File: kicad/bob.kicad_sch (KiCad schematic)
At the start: 45 parts, among them J1 GPIO (Optional), J2 Mini USB Female, J3 Battery Connector, J4 GPIO (Optional), SW1 Screw Switch, U1 RP2040, U2 W25Q64JVSS, U3 NCP1117-3.3_SOT223, U4 MPU-6050, Y1 12MHz

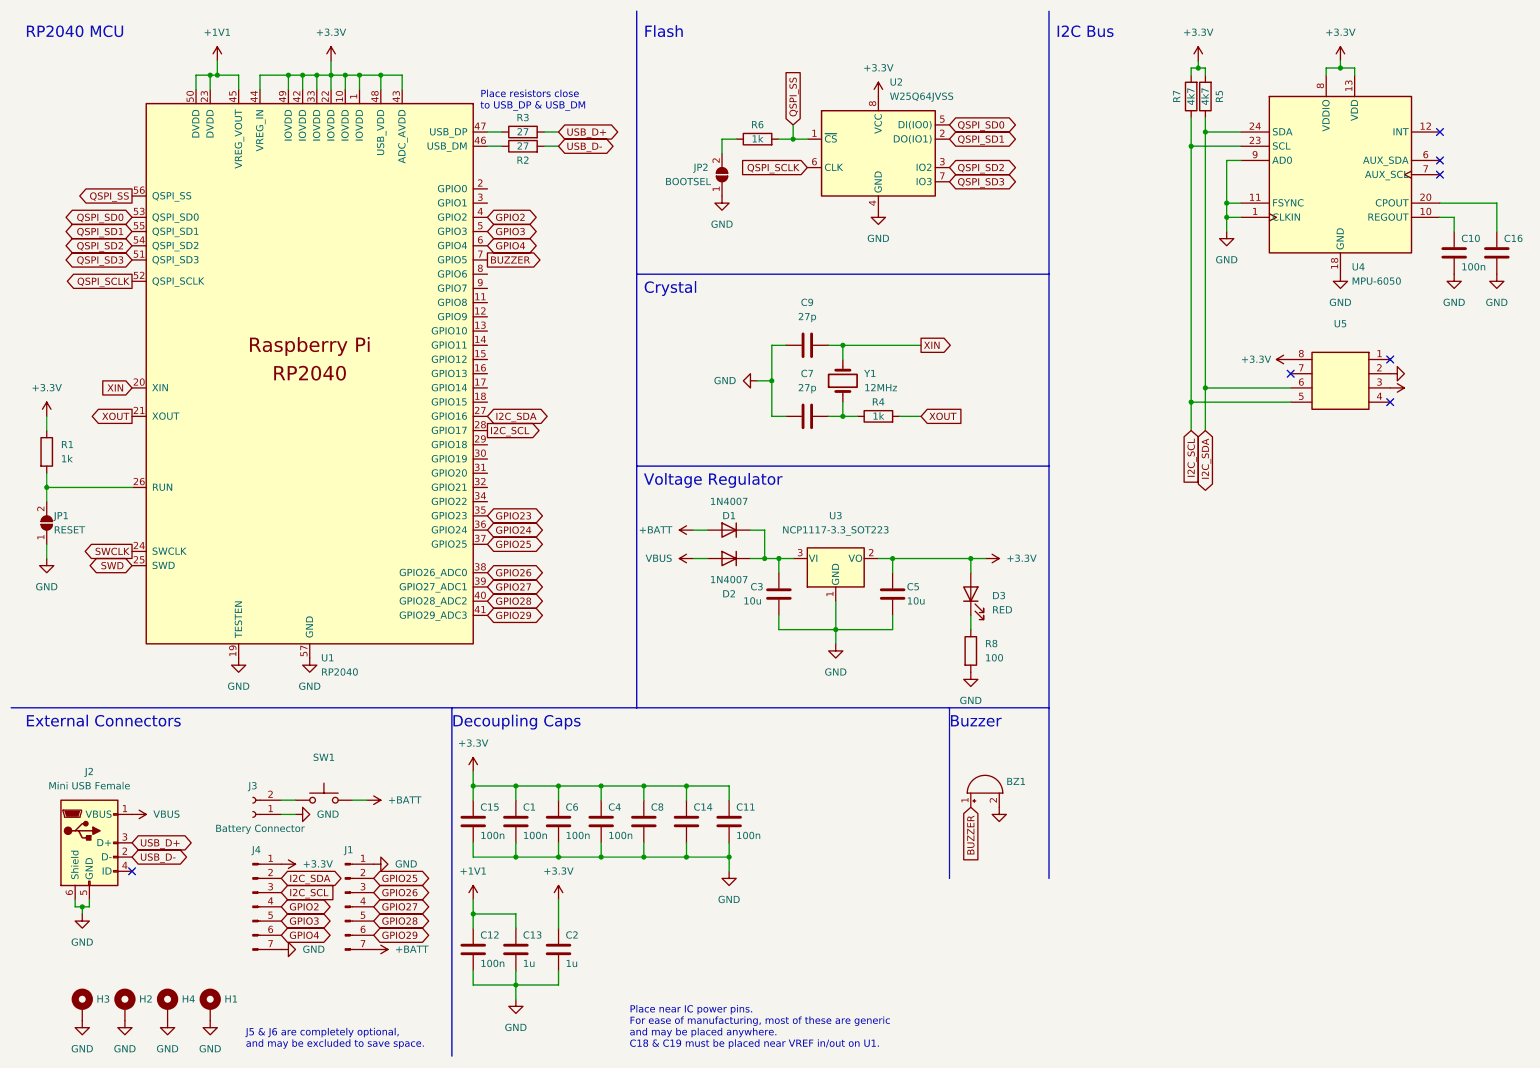
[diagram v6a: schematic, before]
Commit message: Added SWD connector and test points
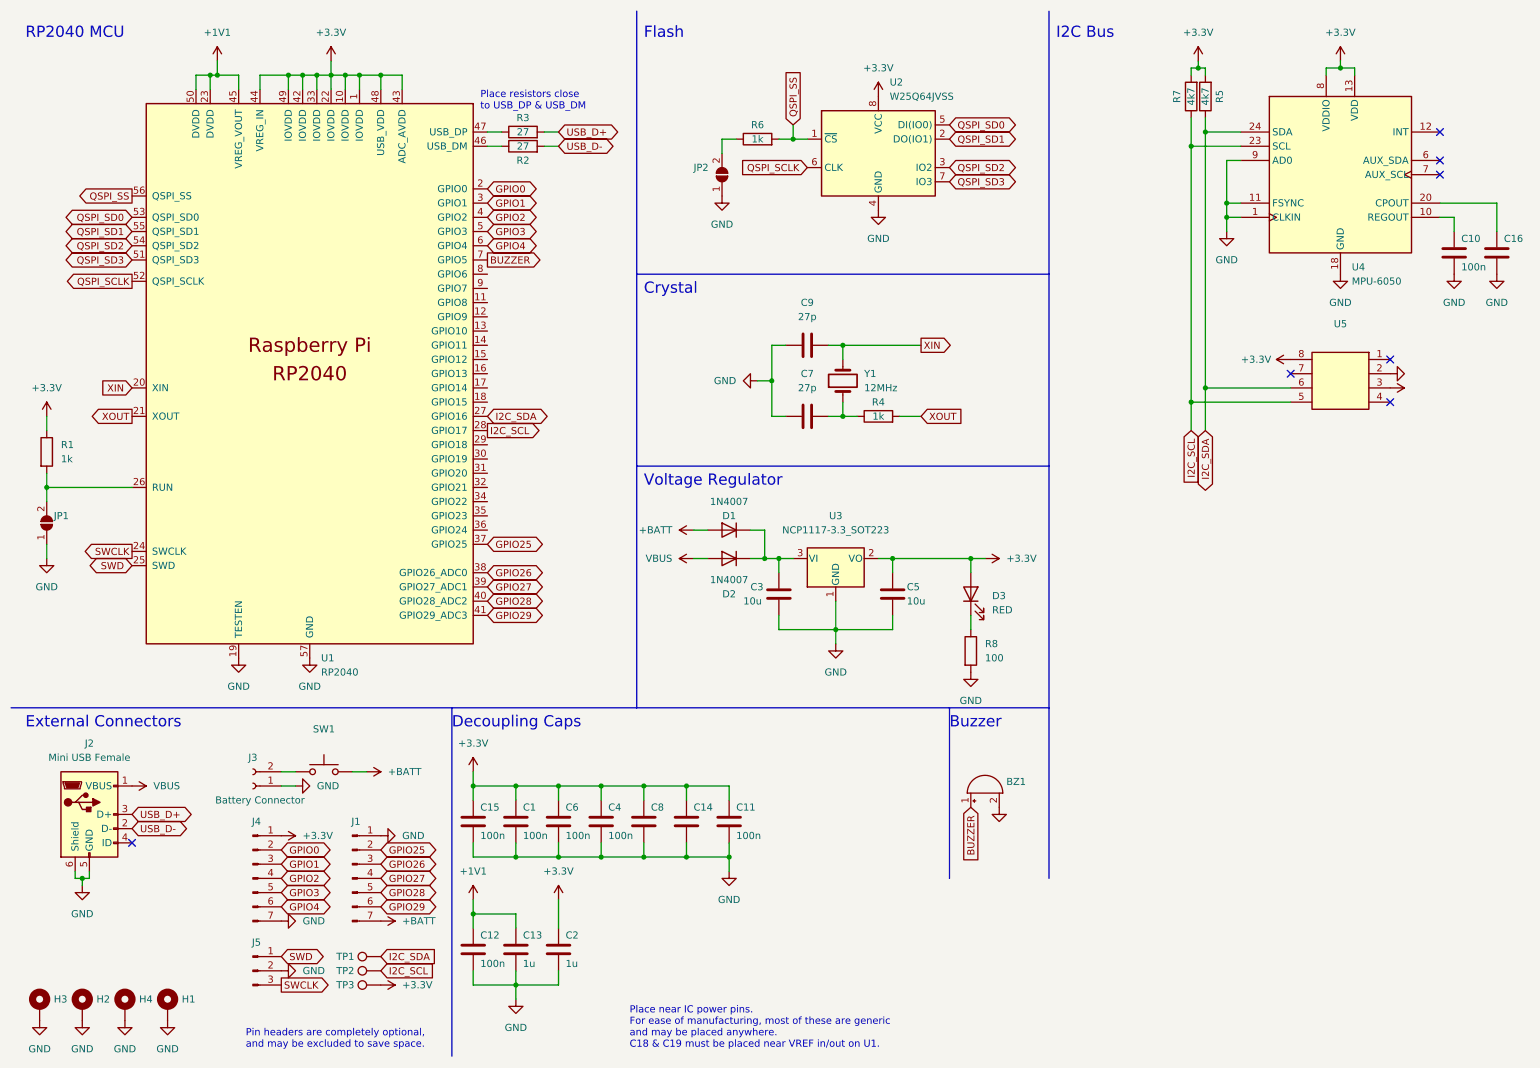
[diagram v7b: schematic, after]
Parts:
- added J5: (no value), symbol Connector:Conn_01x03_Male
- added TP1, TP2, TP3: (no value), symbol Connector:TestPoint
- C1, C10, C11, C12, C13, C15, C2, C4, C6, C7, C9: footprint Capacitor_SMD:C_0402_1005Metric -> (none)
- JP1: value RESET -> (none); footprint Jumper:SolderJumper-2_P1.3mm_Open_TrianglePad1.0x1.5mm -> (none)
- JP2: value BOOTSEL -> (none); footprint Jumper:SolderJumper-2_P1.3mm_Open_TrianglePad1.0x1.5mm -> (none)
- R1, R2, R3, R4, R5, R6, R7, R8: footprint Resistor_SMD:R_0402_1005Metric -> (none)
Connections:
- net +3V3: now also TP3.1
- net GND: now also J5.2 (Pin_2)
- net I2C_SCL: now also TP2.1; no longer J4.3 (Pin_3)
- net I2C_SDA: now also TP1.1; no longer J4.2 (Pin_2)
- net SWCLK: now also J5.3 (Pin_3)
- net SWD: now also J5.1 (Pin_1)
- net GPIO0: now reaches U1.2 (GPIO0)
- net GPIO0: now also J4.2 (Pin_2)
- net GPIO1: now reaches U1.3 (GPIO1)
- net GPIO1: now also J4.3 (Pin_3)
- net GPIO23: no longer names the net of U1.35 (GPIO23)
- net GPIO24: no longer names the net of U1.36 (GPIO24)
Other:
- note added: "Pin headers are completely optional, and may be excluded to save space."
- note removed: "J5 & J6 are completely optional, and may be excluded to save space."
- moved on the sheet: H1, H2, H3, H4, J1, J2, J3, J4, SW1

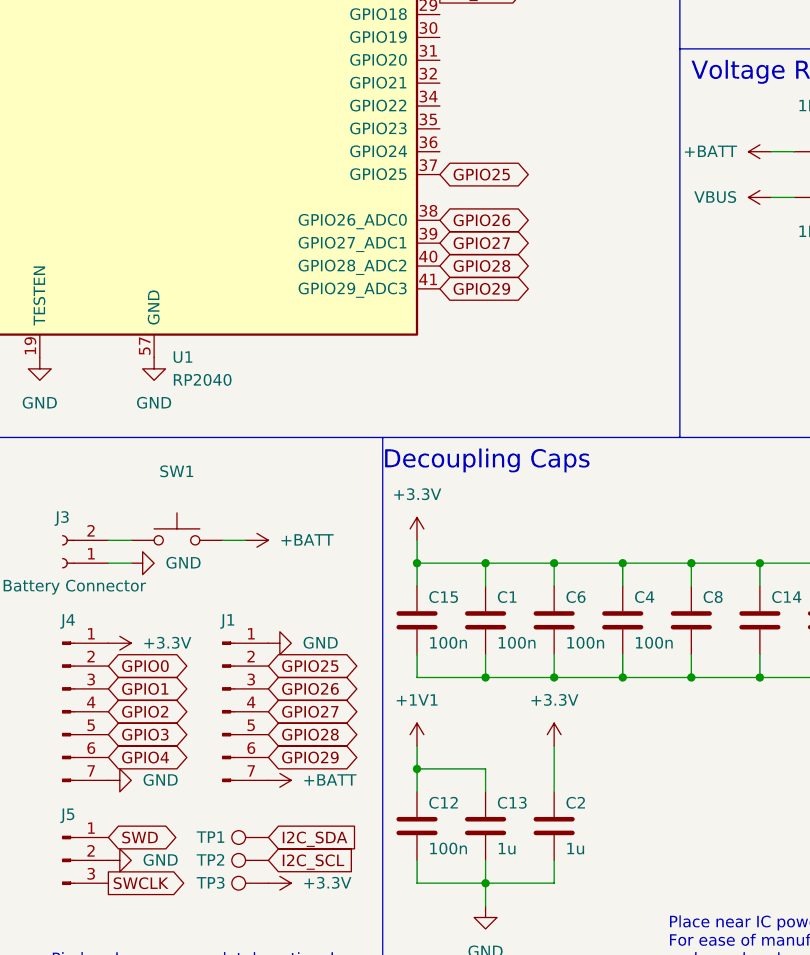
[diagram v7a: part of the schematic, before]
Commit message: Broke out VBAT
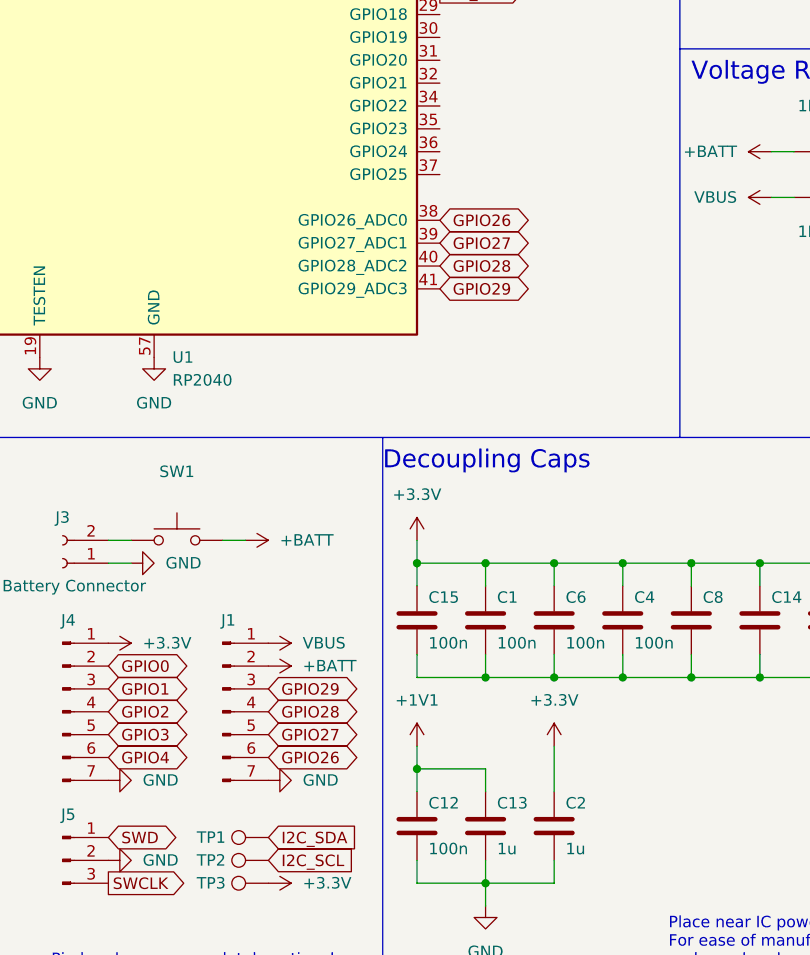
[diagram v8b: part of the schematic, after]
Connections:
- net +BATT: now also J1.2 (Pin_2); no longer J1.7 (Pin_7)
- net GND: now also J1.7 (Pin_7); no longer J1.1 (Pin_1)
- net GPIO26: now also J1.6 (Pin_6); no longer J1.3 (Pin_3)
- net GPIO27: now also J1.5 (Pin_5); no longer J1.4 (Pin_4)
- net GPIO28: now also J1.4 (Pin_4); no longer J1.5 (Pin_5)
- net GPIO29: now also J1.3 (Pin_3); no longer J1.6 (Pin_6)
- net VBUS: now also J1.1 (Pin_1)
- net GPIO25: no longer names the net of U1.37 (GPIO25)
- net GPIO25: no longer J1.2 (Pin_2)
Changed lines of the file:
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@@
+    )
+  )
+  (global_label "GPIO26" (shape bidirectional) (at 76.2 171.45 0) (fields_autoplaced)
+    (effects (font (size 1.27 1.27)) (justify left))
+    (property "Intersheet References" "${INTERSHEET_REFS}" (id 0) (at 85.5074 171.5294 0)
+      (effects (font (size 1.27 1.27)) (justify left) hide)
     )
   )
@@
     )
   )
-  (global_label "GPIO29" (shape bidirectional) (at 76.2 171.45 0) (fields_autoplaced)
-    (effects (font (size 1.27 1.27)) (justify left))
-    (property "Intersheet References" "${INTERSHEET_REFS}" (id 0) (at 85.5074 171.3706 0)
-      (effects (font (size 1.27 1.27)) (justify left) hide)
-    )
-  )
   (global_label "GPIO0" (shape bidirectional) (at 95.25 43.18 0) (fields_autoplaced)
     (effects (font (size 1.27 1.27)) (justify left))
     (property "Intersheet References" "${INTERSHEET_REFS}" (id 0) (at 103.3479 43.1006 0)
-      (effects (font (size 1.27 1.27)) (justify left) hide)
-    )
-  )
-  (global_label "GPIO25" (shape bidirectional) (at 76.2 161.29 0) (fields_autoplaced)
-    (effects (font (size 1.27 1.27)) (justify left))
-    (property "Intersheet References" "${INTERSHEET_REFS}" (id 0) (at 85.5074 161.2106 0)
       (effects (font (size 1.27 1.27)) (justify left) hide)
     )
@@
     )
   )
+  (global_label "GPIO28" (shape bidirectional) (at 76.2 166.37 0) (fields_autoplaced)
+    (effects (font (size 1.27 1.27)) (justify left))
+    (property "Intersheet References" "${INTERSHEET_REFS}" (id 0) (at 85.5074 166.4494 0)
+      (effects (font (size 1.27 1.27)) (justify left) hide)
+    )
+  )
   (global_label "QSPI_SS" (shape input) (at 149.86 31.75 90) (fields_autoplaced)
     (effects (font (size 1.27 1.27)) (justify left))
@@
     (effects (font (size 1.27 1.27)) (justify left))
     (property "Intersheet References" "${INTERSHEET_REFS}" (id 0) (at 104.5574 119.3006 0)
-      (effects (font (size 1.27 1.27)) (justify left) hide)
-    )
-  )
-  (global_label "GPIO26" (shape bidirectional) (at 76.2 163.83 0) (fields_autoplaced)
-    (effects (font (size 1.27 1.27)) (justify left))
-    (property "Intersheet References" "${INTERSHEET_REFS}" (id 0) (at 85.5074 163.7506 0)
       (effects (font (size 1.27 1.27)) (justify left) hide)
     )
@@
     )
   )
+  (global_label "GPIO27" (shape bidirectional) (at 76.2 168.91 0) (fields_autoplaced)
+    (effects (font (size 1.27 1.27)) (justify left))
+    (property "Intersheet References" "${INTERSHEET_REFS}" (id 0) (at 85.5074 168.9894 0)
+      (effects (font (size 1.27 1.27)) (justify left) hide)
+    )
+  )
   (global_label "QSPI_SD1" (shape bidirectional) (at 31.75 50.8 180) (fields_autoplaced)
     (effects (font (size 1.27 1.27)) (justify right))
@@
     )
   )
+  (global_label "GPIO29" (shape bidirectional) (at 76.2 163.83 0) (fields_autoplaced)
+    (effects (font (size 1.27 1.27)) (justify left))
+    (property "Intersheet References" "${INTERSHEET_REFS}" (id 0) (at 85.5074 163.7506 0)
+      (effects (font (size 1.27 1.27)) (justify left) hide)
+    )
+  )
   (global_label "GPIO3" (shape bidirectional) (at 58.42 168.91 0) (fields_autoplaced)
     (effects (font (size 1.27 1.27)) (justify left))
@@
     )
   )
-  (global_label "GPIO27" (shape bidirectional) (at 76.2 166.37 0) (fields_autoplaced)
-    (effects (font (size 1.27 1.27)) (justify left))
-    (property "Intersheet References" "${INTERSHEET_REFS}" (id 0) (at 85.5074 166.2906 0)
-      (effects (font (size 1.27 1.27)) (justify left) hide)
-    )
-  )
   (global_label "GPIO4" (shape bidirectional) (at 95.25 53.34 0) (fields_autoplaced)
     (effects (font (size 1.27 1.27)) (justify left))
@@
     )
   )
-  (global_label "GPIO25" (shape bidirectional) (at 95.25 106.68 0) (fields_autoplaced)
-    (effects (font (size 1.27 1.27)) (justify left))
-    (property "Intersheet References" "${INTERSHEET_REFS}" (id 0) (at 104.5574 106.6006 0)
-      (effects (font (size 1.27 1.27)) (justify left) hide)
-    )
-  )
   (global_label "SWCLK" (shape output) (at 31.75 107.95 180) (fields_autoplaced)
     (effects (font (size 1.27 1.27)) (justify right))
@@
     (effects (font (size 1.27 1.27)) (justify left))
     (property "Intersheet References" "${INTERSHEET_REFS}" (id 0) (at 66.5179 161.2106 0)
-      (effects (font (size 1.27 1.27)) (justify left) hide)
-    )
-  )
-  (global_label "GPIO28" (shape bidirectional) (at 76.2 168.91 0) (fields_autoplaced)
-    (effects (font (size 1.27 1.27)) (justify left))
-    (property "Intersheet References" "${INTERSHEET_REFS}" (id 0) (at 85.5074 168.8306 0)
       (effects (font (size 1.27 1.27)) (justify left) hide)
     )
@@
     (pin "2")
   )
-  (symbol (lib_id "power:+BATT") (at 76.2 173.99 270) (unit 1)
-    (in_bom yes) (on_board yes) (fields_autoplaced)
-    (property "Reference" "#PWR0124" (id 0) (at 72.39 173.99 0)
-      (effects (font (size 1.27 1.27)) hide)
-    )
-    (property "Value" "+BATT" (id 1) (at 80.01 173.9899 90)
-      (effects (font (size 1.27 1.27)) (justify left))
-    )
-    (property "Footprint" "" (id 2) (at 76.2 173.99 0)
-      (effects (font (size 1.27 1.27)) hide)
-    )
-    (property "Datasheet" "" (id 3) (at 76.2 173.99 0)
+  (symbol (lib_id "power:+BATT") (at 76.2 161.29 270) (mirror x) (unit 1)
+    (in_bom yes) (on_board yes) (fields_autoplaced)
+    (property "Reference" "#PWR0124" (id 0) (at 72.39 161.29 0)
+      (effects (font (size 1.27 1.27)) hide)
+    )
+    (property "Value" "+BATT" (id 1) (at 80.01 161.2901 90)
+      (effects (font (size 1.27 1.27)) (justify left))
+    )
+    (property "Footprint" "" (id 2) (at 76.2 161.29 0)
+      (effects (font (size 1.27 1.27)) hide)
+    )
+    (property "Datasheet" "" (id 3) (at 76.2 161.29 0)
       (effects (font (size 1.27 1.27)) hide)
     )
@@
     (pin "2")
   )
-  (symbol (lib_id "power:GND") (at 76.2 158.75 90) (unit 1)
-    (in_bom yes) (on_board yes) (fields_autoplaced)
-    (property "Reference" "#PWR0127" (id 0) (at 82.55 158.75 0)
-      (effects (font (size 1.27 1.27)) hide)
-    )
-    (property "Value" "GND" (id 1) (at 80.01 158.7499 90)
+  (symbol (lib_id "power:GND") (at 76.2 173.99 90) (mirror x) (unit 1)
+    (in_bom yes) (on_board yes) (fields_autoplaced)
+    (property "Reference" "#PWR0127" (id 0) (at 82.55 173.99 0)
+      (effects (font (size 1.27 1.27)) hide)
+    )
+    (property "Value" "GND" (id 1) (at 80.01 173.9901 90)
       (effects (font (size 1.27 1.27)) (justify right))
     )
-    (property "Footprint" "" (id 2) (at 76.2 158.75 0)
-      (effects (font (size 1.27 1.27)) hide)
-    )
-    (property "Datasheet" "" (id 3) (at 76.2 158.75 0)
+    (property "Footprint" "" (id 2) (at 76.2 173.99 0)
+      (effects (font (size 1.27 1.27)) hide)
+    )
+    (property "Datasheet" "" (id 3) (at 76.2 173.99 0)
       (effects (font (size 1.27 1.27)) hide)
     )
@@
   (symbol (lib_id "power:+3.3V") (at 76.2 185.42 270) (unit 1)
     (in_bom yes) (on_board yes) (fields_autoplaced)
-    (property "Reference" "#PWR?" (id 0) (at 72.39 185.42 0)
+    (property "Reference" "#PWR0144" (id 0) (at 72.39 185.42 0)
       (effects (font (size 1.27 1.27)) hide)
     )
@@
     (pin "3")
   )
+  (symbol (lib_id "power:VBUS") (at 76.2 158.75 270) (unit 1)
+    (in_bom yes) (on_board yes) (fields_autoplaced)
+    (property "Reference" "#PWR0145" (id 0) (at 72.39 158.75 0)
+      (effects (font (size 1.27 1.27)) hide)
+    )
+    (property "Value" "VBUS" (id 1) (at 80.01 158.7499 90)
+      (effects (font (size 1.27 1.27)) (justify left))
+    )
+    (property "Footprint" "" (id 2) (at 76.2 158.75 0)
+      (effects (font (size 1.27 1.27)) hide)
+    )
+    (property "Datasheet" "" (id 3) (at 76.2 158.75 0)
+      (effects (font (size 1.27 1.27)) hide)
+    )
+    (pin "1")
+  )
   (symbol (lib_id "power:GND") (at 100.33 187.96 0) (unit 1)
     (in_bom yes) (on_board yes) (fields_autoplaced)
@@
   (symbol (lib_id "power:GND") (at 58.42 182.88 90) (unit 1)
     (in_bom yes) (on_board yes) (fields_autoplaced)
-    (property "Reference" "#PWR?" (id 0) (at 64.77 182.88 0)
+    (property "Reference" "#PWR0143" (id 0) (at 64.77 182.88 0)
       (effects (font (size 1.27 1.27)) hide)
     )
@@
       (reference "#PWR0142") (unit 1) (value "+3.3V") (footprint "")
     )
+    (path "/f8cba525-0636-43d8-80db-278379ac8bce"
+      (reference "#PWR0143") (unit 1) (value "GND") (footprint "")
+    )
     (path "/ed8ac756-1c98-4fb1-9625-1ecc9897a8f4"
-      (reference "#PWR?") (unit 1) (value "+3.3V") (footprint "")
-    )
-    (path "/f8cba525-0636-43d8-80db-278379ac8bce"
-      (reference "#PWR?") (unit 1) (value "GND") (footprint "")
+      (reference "#PWR0144") (unit 1) (value "+3.3V") (footprint "")
+    )
+    (path "/ef8eae57-90ce-4cd1-99f6-6aba1fb0e654"
+      (reference "#PWR0145") (unit 1) (value "VBUS") (footprint "")
     )
     (path "/e65ef186-5520-4142-8b10-d2898e4cdc2f"
@@
     )
     (path "/3013c0f4-fe26-473e-9442-7b1a93e136c9"
-      (reference "J5") (unit 1) (value "Conn_01x03_Male") (footprint "")
+      (reference "J5") (unit 1) (value "Conn_01x03_Male") (footprint "Connector_PinHeader_2.54mm:PinHeader_1x03_P2.54mm_Vertical")
     )
     (path "/0111ad60-beec-4fdd-bf52-89c00a0b04af"
@@
     )
     (path "/d1910422-7ae9-42c3-aa16-3778d69d2211"
-      (reference "U5") (unit 1) (value "HP203B") (footprint "")
+      (reference "U5") (unit 1) (value "HP203B") (footprint "RP2040_minimal:LGA-8_3.6x3.8x0.9P")
     )
     (path "/e9d165af-abdf-49f9-beea-a51c27a6ec26"
